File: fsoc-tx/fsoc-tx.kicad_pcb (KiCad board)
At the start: 4 copper layers, 52 x 40 mm, 52 parts, among them J1 USB4105-GF-A, J2 B8B-PH-K-S, J3 FTSH-105-01-L-DV-K, J4 B3B-PH-K-S, J5 Conn_01x03, SW1 SW_RESET, SW2 USB_BOOT, SW3 SW_DPST, U1 USBLC6-2SC6, U2 AP2112K-3.3, U3 RP2354A, U4 74AHCT1G125, U5 TPS22919DCK, Y1 ABM8-272-T3, Y2 ASTX-H11-10.000MHz-T

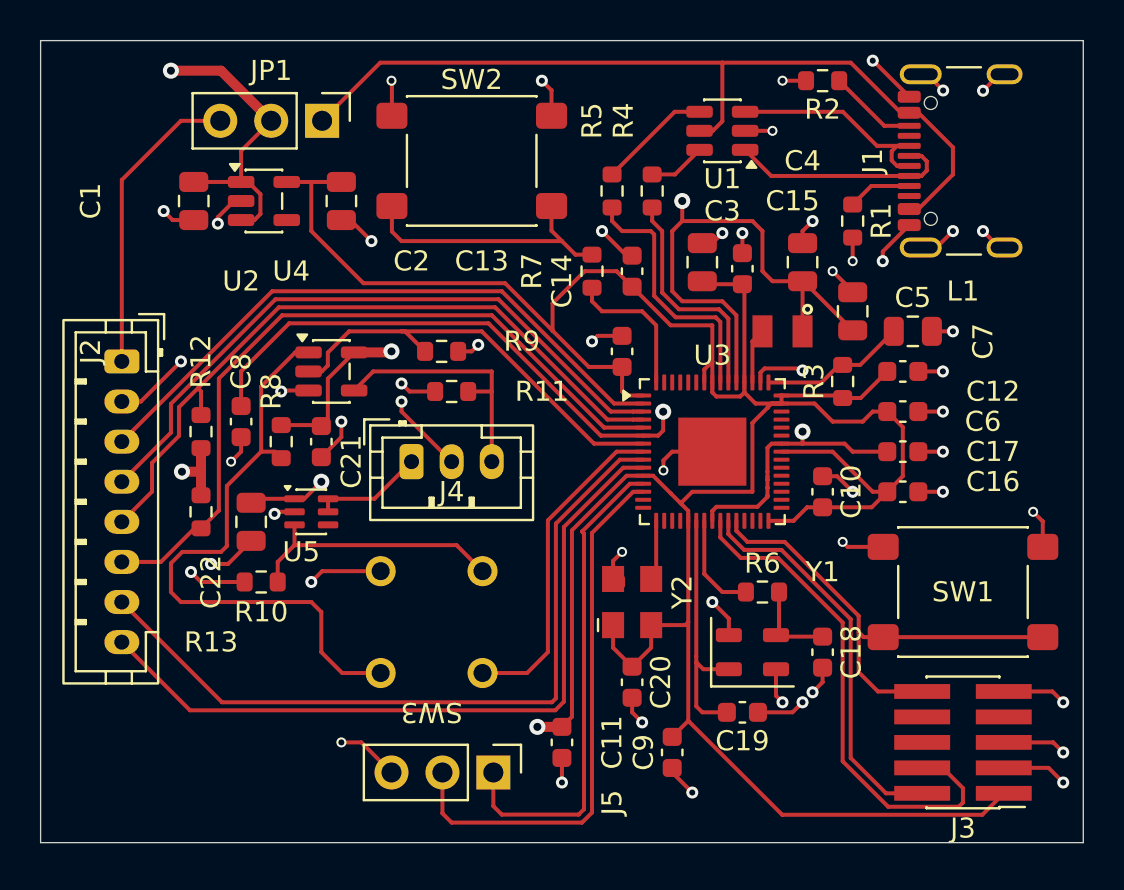
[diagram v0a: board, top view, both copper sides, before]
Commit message: TX PCB: checkpoint (error: non-plated through holes of GCT USB4105 has 0.194mm distance of the copper pads while the board steup is set to 0.25mm.. waiting approval)
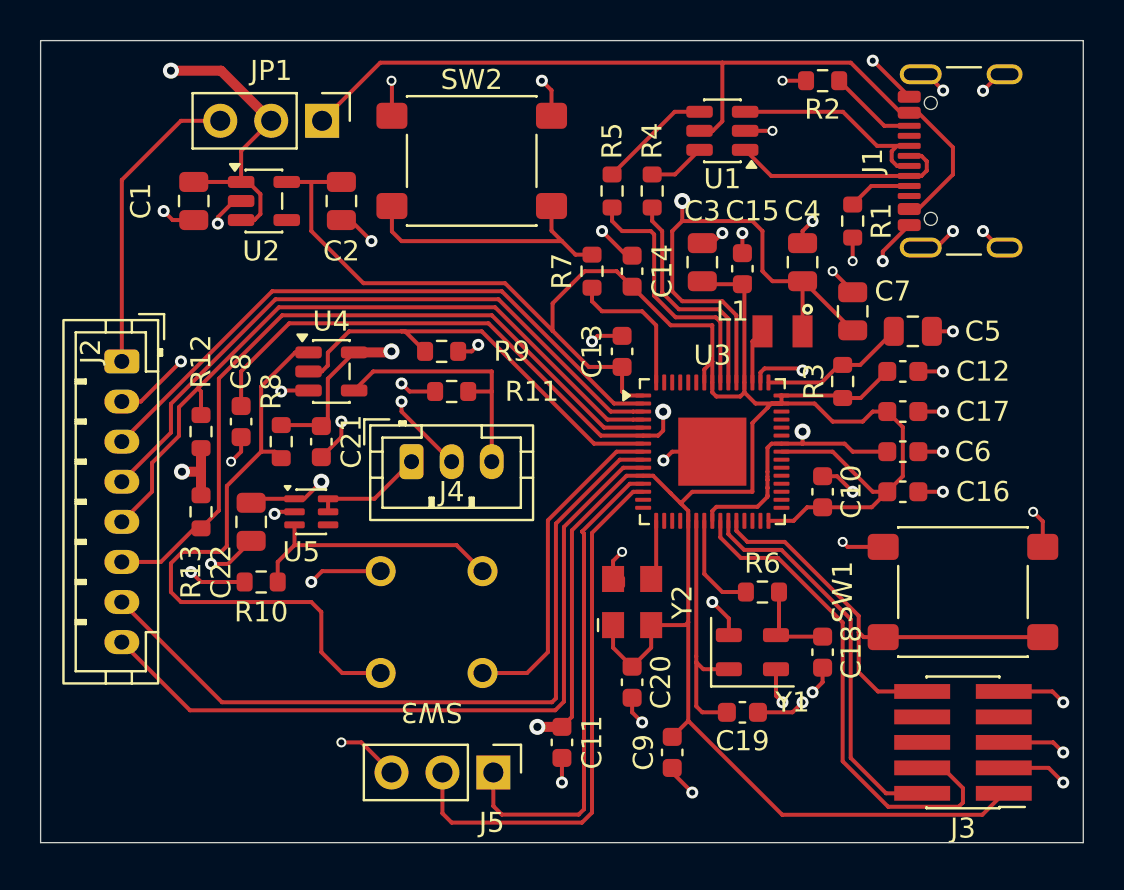
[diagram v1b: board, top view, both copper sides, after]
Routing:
- net GND: track 103.2 -> 102.7 mm
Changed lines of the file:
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@@
 		(tags "capacitor")
 		(property "Reference" "C11"
-			(at 0 2.5 90)
+			(at 0 1.5 90)
 			(layer "F.SilkS")
 			(effects
@@
 		(tags "capacitor")
 		(property "Reference" "C13"
-			(at -4.5 7 0)
+			(at 0 1.5 90)
 			(layer "F.SilkS")
 			(effects
@@
 		(tags "resistor")
 		(property "Reference" "R4"
-			(at 3.5 -1.43 90)
+			(at 2.5 0 90)
 			(layer "F.SilkS")
 			(effects
@@
 		(tags "capacitor")
 		(property "Reference" "C7"
-			(at -1.5 6.5 90)
+			(at 1 2 0)
 			(layer "F.SilkS")
 			(effects
@@
 		(tags "Through hole pin header THT 1x03 2.54mm single row")
 		(property "Reference" "J5"
-			(at 1.5 -5.92 90)
+			(at 2.5 0.08 0)
 			(layer "F.SilkS")
 			(effects
@@
 		(tags "capacitor")
 		(property "Reference" "C21"
-			(at -1 1.5 90)
+			(at 0 1.5 90)
 			(layer "F.SilkS")
 			(effects
@@
 		(tags "capacitor")
 		(property "Reference" "C14"
-			(at 0.5 3.5 90)
+			(at 0 -1.5 90)
 			(layer "F.SilkS")
 			(effects
@@
 		(tags "SOT TO_SOT_SMD")
 		(property "Reference" "U4"
-			(at -2 -5 0)
+			(at 0 -2.5 0)
 			(layer "F.SilkS")
 			(effects
@@
 		(tags "capacitor")
 		(property "Reference" "C22"
-			(at 3 2 90)
+			(at 2.5 1.5 90)
 			(layer "F.SilkS")
 			(effects
@@
 		(tags "capacitor")
 		(property "Reference" "C12"
-			(at -4.5 -1 0)
+			(at -4 0 0)
 			(layer "F.SilkS")
 			(effects
@@
 		(tags "capacitor")
 		(property "Reference" "C2"
-			(at 3 -3.5 0)
+			(at 2.5 0 0)
 			(layer "F.SilkS")
 			(effects
@@
 		(tags "capacitor")
 		(property "Reference" "C4"
-			(at 5.05 0 0)
+			(at 2.55 0 0)
 			(layer "F.SilkS")
 			(effects
@@
 		(tags "resistor")
 		(property "Reference" "R5"
-			(at 3.5 -1 90)
+			(at 2.5 0 90)
 			(layer "F.SilkS")
 			(effects
@@
 		(tags "resistor")
 		(property "Reference" "R11"
-			(at -4.5 0 0)
+			(at -4 0 0)
 			(layer "F.SilkS")
 			(effects
@@
 		(at 131 127.5 90)
 		(property "Reference" "Y2"
-			(at 0.5 2.5 90)
+			(at 0 2.5 90)
 			(unlocked yes)
 			(layer "F.SilkS")
@@
 		(tags "capacitor")
 		(property "Reference" "C15"
-			(at -3.375 -2.5 0)
+			(at -2.875 -0.5 0)
 			(layer "F.SilkS")
 			(effects
@@
 		(at 138.5 114)
 		(property "Reference" "L1"
-			(at 9 -2 0)
+			(at -2.5 -1 0)
 			(unlocked yes)
 			(layer "F.SilkS")
@@
 		(tags "resistor")
 		(property "Reference" "R13"
-			(at 6.5 -0.5 0)
+			(at 3 0.5 90)
 			(layer "F.SilkS")
 			(effects
@@
 		(tags "capacitor")
 		(property "Reference" "C6"
-			(at 4 -1.5 0)
+			(at 3.5 0 0)
 			(layer "F.SilkS")
 			(effects
@@
 		(tags "ABM8 Abracon crystal 3225 3.2x2.5")
 		(property "Reference" "Y1"
-			(at 3.5 -4 0)
+			(at 2 2.5 0)
 			(layer "F.SilkS")
 			(effects
@@
 		(tags "SPST Button Switch CK C&K")
 		(property "Reference" "SW1"
-			(at 0 0 0)
+			(at 6 0 270)
 			(layer "F.SilkS")
 			(effects
@@
 		(tags "resistor")
 		(property "Reference" "R9"
-			(at 4 -0.5 0)
+			(at 3.5 0 0)
 			(layer "F.SilkS")
 			(effects
@@
 		(tags "resistor")
 		(property "Reference" "R7"
-			(at 0 3 90)
+			(at 0 1.5 90)
 			(layer "F.SilkS")
 			(effects
@@
 		(tags "capacitor")
 		(property "Reference" "C3"
-			(at 2.55 1 0)
+			(at 2.55 0 0)
 			(layer "F.SilkS")
 			(effects
@@
 		(tags "SOT TO_SOT_SMD")
 		(property "Reference" "U2"
-			(at -1.1375 4 0)
+			(at -0.1375 2.5 0)
 			(layer "F.SilkS")
 			(effects
@@
 		(tags "capacitor")
 		(property "Reference" "C16"
-			(at -4.5 0.5 0)
+			(at -4 0 0)
 			(layer "F.SilkS")
 			(effects
@@
 		(tags "capacitor")
 		(property "Reference" "C17"
-			(at -4.5 -2 0)
+			(at -4 0 0)
 			(layer "F.SilkS")
 			(effects
@@
 		(tags "capacitor")
 		(property "Reference" "C1"
-			(at 0 5.1375 90)
+			(at 0 2.6375 90)
 			(layer "F.SilkS")
 			(effects
@@
 		(tags "capacitor")
 		(property "Reference" "C5"
-			(at 0 -1.68 0)
+			(at 3.5 0 0)
 			(layer "F.SilkS")
 			(effects
@@
 	)
 	(segment
+		(start 132.562089 120.437911)
+		(end 133 120)
+		(width 0.2)
+		(layer "F.Cu")
+		(net "GND")
+	)
+	(segment
 		(start 151.77 135.77)
 		(end 152.5 136.5)
@@
 	)
 	(segment
-		(start 133 120)
-		(end 132.562089 120.437911)
-		(width 0.2)
-		(layer "F.Cu")
-		(net "GND")
-	)
-	(segment
 		(start 137.60364 115.85)
 		(end 139.4 115.85)
@@
 	)
 	(segment
-		(start 132.562089 120.437911)
-		(end 132.562089 120.937911)
-		(width 0.2)
-		(layer "F.Cu")
-		(net "GND")
-	)
-	(segment
 		(start 133 135.775)
 		(end 133.225 135.775)
@@
 	)
 	(segment
-		(start 135 120)
-		(end 133 120)
-		(width 0.2)
-		(layer "F.Cu")
-		(net "GND")
-	)
-	(segment
 		(start 137.4 116.05364)
 		(end 137.60364 115.85)
@@
 	)
 	(segment
+		(start 133 120)
+		(end 135 120)
+		(width 0.2)
+		(layer "F.Cu")
+		(net "GND")
+	)
+	(segment
 		(start 141.225 121.225)
 		(end 142 122)
@@
 	)
 	(via
-		(at 132.562089 120.937911)
-		(size 0.5)
+		(at 132.562089 120.437911)
+		(size 0.6)
 		(drill 0.3)
 		(layers "F.Cu" "B.Cu")
